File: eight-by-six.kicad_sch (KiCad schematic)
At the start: 98 parts, among them J1 Left, J2 Right, SW1 Key, SW10 Key, SW11 Key, SW12 Key, SW13 Key, SW14 Key, SW15 Key, SW16 Key, SW17 Key, SW18 Key, SW19 Key, SW2 Key, SW20 Key, SW21 Key, SW22 Key, SW23 Key, SW24 Key, SW25 Key, SW26 Key, SW27 Key, SW28 Key, SW29 Key, SW3 Key, SW30 Key, SW31 Key, SW32 Key, SW33 Key, SW34 Key, SW35 Key, SW36 Key, SW37 Key, SW38 Key, SW39 Key, SW4 Key, SW40 Key, SW41 Key, SW42 Key, SW43 Key, SW44 Key, SW45 Key, SW46 Key, SW47 Key, SW48 Key, SW5 Key, SW6 Key, SW7 Key, SW8 Key, SW9 Key

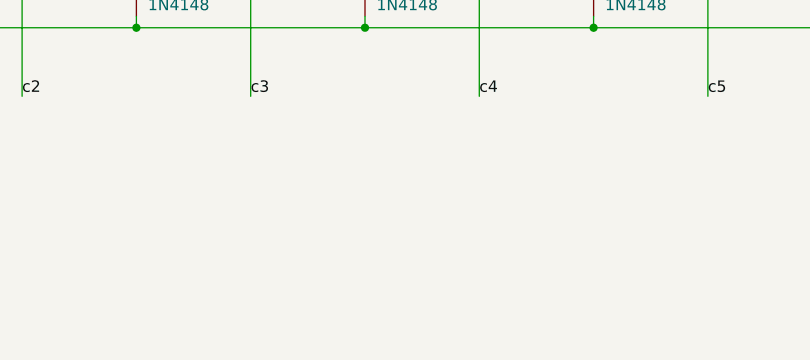
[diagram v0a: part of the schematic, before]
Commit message: add mounting holes, fixe shape, connector position, proto-traces from the connector
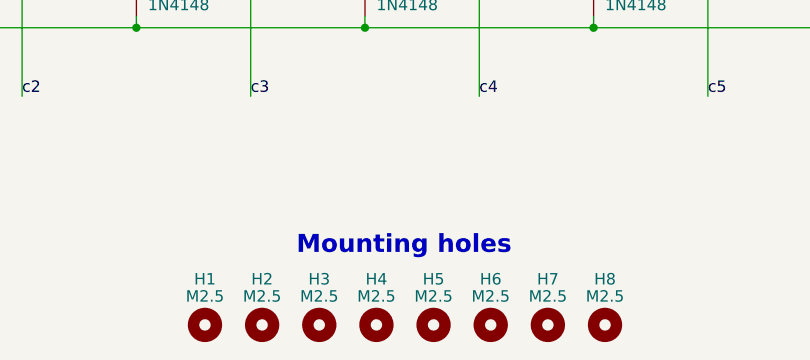
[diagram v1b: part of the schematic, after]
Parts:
- added H1, H2, H3, H4, H5, H6, H7, H8: M2.5, MountingHole:MountingHole_2.7mm_M2.5, symbol Mechanical:MountingHole
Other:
- note added: "Mounting holes"
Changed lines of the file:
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@@
     (effects (font (size 1.27 1.27)) (justify left bottom))
+  )
+  (text "Mounting holes" (at 106.68 182.88 0)
+    (effects (font (size 2 2) (thickness 0.4) bold) (justify left bottom))
   )
   (text "RESERVED (GPIO)" (at 242.57 76.2 0)
@@
         (path "/b652f545-e833-471c-a9a7-1cc191b8a73a"
           (reference "#PWR01") (unit 1)
+        )
+      )
+    )
+  )
+  (symbol (lib_id "Mechanical:MountingHole") (at 96.52 190.5 0) (unit 1)
+    (in_bom yes) (on_board yes) (dnp no)
+    (property "Reference" "H1" (at 96.52 185.42 0)
+      (effects (font (size 1.27 1.27)))
+    )
+    (property "Value" "M2.5" (at 96.52 187.325 0)
+      (effects (font (size 1.27 1.27)))
+    )
+    (property "Footprint" "MountingHole:MountingHole_2.7mm_M2.5" (at 96.52 190.5 0)
+      (effects (font (size 1.27 1.27)) hide)
+    )
+    (property "Datasheet" "~" (at 96.52 190.5 0)
+      (effects (font (size 1.27 1.27)) hide)
+    )
+    (instances
+      (project "eight-by-six"
+        (path "/b652f545-e833-471c-a9a7-1cc191b8a73a"
+          (reference "H1") (unit 1)
         )
       )
@@
     )
   )
+  (symbol (lib_id "Mechanical:MountingHole") (at 115.57 190.5 0) (unit 1)
+    (in_bom yes) (on_board yes) (dnp no)
+    (property "Reference" "H4" (at 115.57 185.42 0)
+      (effects (font (size 1.27 1.27)))
+    )
+    (property "Value" "M2.5" (at 115.57 187.325 0)
+      (effects (font (size 1.27 1.27)))
+    )
+    (property "Footprint" "MountingHole:MountingHole_2.7mm_M2.5" (at 115.57 190.5 0)
+      (effects (font (size 1.27 1.27)) hide)
+    )
+    (property "Datasheet" "~" (at 115.57 190.5 0)
+      (effects (font (size 1.27 1.27)) hide)
+    )
+    (instances
+      (project "eight-by-six"
+        (path "/b652f545-e833-471c-a9a7-1cc191b8a73a"
+          (reference "H4") (unit 1)
+        )
+      )
+    )
+  )
+  (symbol (lib_id "Mechanical:MountingHole") (at 121.92 190.5 0) (unit 1)
+    (in_bom yes) (on_board yes) (dnp no)
+    (property "Reference" "H5" (at 121.92 185.42 0)
+      (effects (font (size 1.27 1.27)))
+    )
+    (property "Value" "M2.5" (at 121.92 187.325 0)
+      (effects (font (size 1.27 1.27)))
+    )
+    (property "Footprint" "MountingHole:MountingHole_2.7mm_M2.5" (at 121.92 190.5 0)
+      (effects (font (size 1.27 1.27)) hide)
+    )
+    (property "Datasheet" "~" (at 121.92 190.5 0)
+      (effects (font (size 1.27 1.27)) hide)
+    )
+    (instances
+      (project "eight-by-six"
+        (path "/b652f545-e833-471c-a9a7-1cc191b8a73a"
+          (reference "H5") (unit 1)
+        )
+      )
+    )
+  )
+  (symbol (lib_id "Mechanical:MountingHole") (at 109.22 190.5 0) (unit 1)
+    (in_bom yes) (on_board yes) (dnp no)
+    (property "Reference" "H3" (at 109.22 185.42 0)
+      (effects (font (size 1.27 1.27)))
+    )
+    (property "Value" "M2.5" (at 109.22 187.325 0)
+      (effects (font (size 1.27 1.27)))
+    )
+    (property "Footprint" "MountingHole:MountingHole_2.7mm_M2.5" (at 109.22 190.5 0)
+      (effects (font (size 1.27 1.27)) hide)
+    )
+    (property "Datasheet" "~" (at 109.22 190.5 0)
+      (effects (font (size 1.27 1.27)) hide)
+    )
+    (instances
+      (project "eight-by-six"
+        (path "/b652f545-e833-471c-a9a7-1cc191b8a73a"
+          (reference "H3") (unit 1)
+        )
+      )
+    )
+  )
   (symbol (lib_id "Connector_Generic:Conn_01x10") (at 266.7 35.56 0) (unit 1)
     (in_bom yes) (on_board yes) (dnp no)
@@
         )
       )
+    )
+  )
+  (symbol (lib_id "Mechanical:MountingHole") (at 128.27 190.5 0) (unit 1)
+    (in_bom yes) (on_board yes) (dnp no)
+    (property "Reference" "H6" (at 128.27 185.42 0)
+      (effects (font (size 1.27 1.27)))
+    )
+    (property "Value" "M2.5" (at 128.27 187.325 0)
+      (effects (font (size 1.27 1.27)))
+    )
+    (property "Footprint" "MountingHole:MountingHole_2.7mm_M2.5" (at 128.27 190.5 0)
+      (effects (font (size 1.27 1.27)) hide)
+    )
+    (property "Datasheet" "~" (at 128.27 190.5 0)
+      (effects (font (size 1.27 1.27)) hide)
+    )
+    (instances
+      (project "eight-by-six"
+        (path "/b652f545-e833-471c-a9a7-1cc191b8a73a"
+          (reference "H6") (unit 1)
+        )
+      )
+    )
+  )
+  (symbol (lib_id "Mechanical:MountingHole") (at 134.62 190.5 0) (unit 1)
+    (in_bom yes) (on_board yes) (dnp no)
+    (property "Reference" "H7" (at 134.62 185.42 0)
+      (effects (font (size 1.27 1.27)))
+    )
+    (property "Value" "M2.5" (at 134.62 187.325 0)
+      (effects (font (size 1.27 1.27)))
+    )
+    (property "Footprint" "MountingHole:MountingHole_2.7mm_M2.5" (at 134.62 190.5 0)
+      (effects (font (size 1.27 1.27)) hide)
+    )
+    (property "Datasheet" "~" (at 134.62 190.5 0)
+      (effects (font (size 1.27 1.27)) hide)
+    )
+    (instances
+      (project "eight-by-six"
+        (path "/b652f545-e833-471c-a9a7-1cc191b8a73a"
+          (reference "H7") (unit 1)
+        )
+      )
+    )
+  )
+  (symbol (lib_id "Mechanical:MountingHole") (at 140.97 190.5 0) (unit 1)
+    (in_bom yes) (on_board yes) (dnp no)
+    (property "Reference" "H8" (at 140.97 185.42 0)
+      (effects (font (size 1.27 1.27)))
+    )
+    (property "Value" "M2.5" (at 140.97 187.325 0)
+      (effects (font (size 1.27 1.27)))
+    )
+    (property "Footprint" "MountingHole:MountingHole_2.7mm_M2.5" (at 140.97 190.5 0)
+      (effects (font (size 1.27 1.27)) hide)
+    )
+    (property "Datasheet" "~" (at 140.97 190.5 0)
+      (effects (font (size 1.27 1.27)) hide)
+    )
+    (instances
+      (project "eight-by-six"
+        (path "/b652f545-e833-471c-a9a7-1cc191b8a73a"
+          (reference "H8") (unit 1)
+        )
+      )
+    )
+  )
+  (symbol (lib_id "Mechanical:MountingHole") (at 102.87 190.5 0) (unit 1)
+    (in_bom yes) (on_board yes) (dnp no)
+    (property "Reference" "H2" (at 102.87 185.42 0)
+      (effects (font (size 1.27 1.27)))
+    )
+    (property "Value" "M2.5" (at 102.87 187.325 0)
+      (effects (font (size 1.27 1.27)))
+    )
+    (property "Footprint" "MountingHole:MountingHole_2.7mm_M2.5" (at 102.87 190.5 0)
+      (effects (font (size 1.27 1.27)) hide)
+    )
+    (property "Datasheet" "~" (at 102.87 190.5 0)
+      (effects (font (size 1.27 1.27)) hide)
+    )
+    (instances
+      (project "eight-by-six"
+        (path "/b652f545-e833-471c-a9a7-1cc191b8a73a"
+          (reference "H2") (unit 1)
+        )
+      )
